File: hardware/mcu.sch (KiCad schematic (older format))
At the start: 49 parts, among them P3 CONN_01X08_DEBUG, P4 CONN_02X05_JTAG, P5 CONN_01X03_UART, P6 CONN_01X03_CAN, P7 CONN_01X05_ENCODER, SW2 SW_PUSH, U13 TM4C1294KCPDT, U14 74LVCH2T45, U15 SN65HVD231D, Y1 NX5032GA

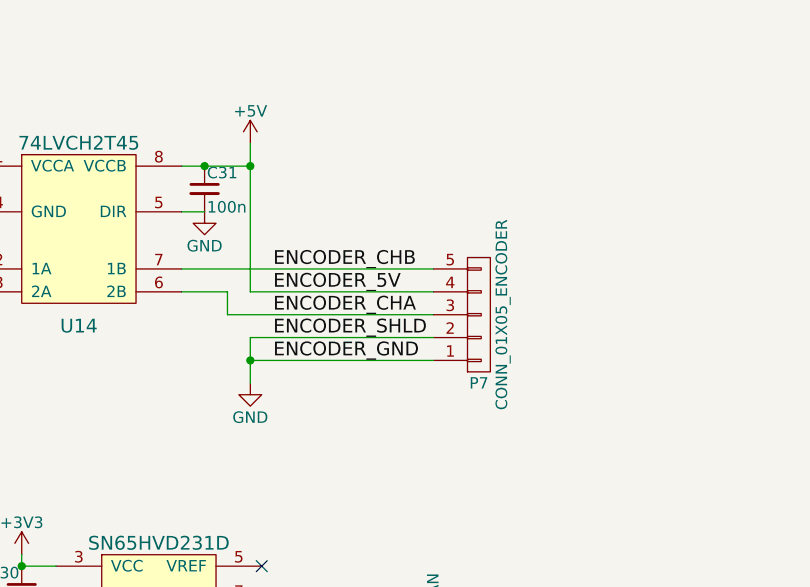
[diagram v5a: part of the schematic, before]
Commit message: Inrush circuit, mounting hole position, temp sensor
- Split inrush circuit (one for each bulk cap). Replaced NTC
  thermistor with 2W power resistor. Replaced D2Pak MOSFET with
  LFPAK MOSFETs.
- Approximate position of mechanical holes chosen.
- Added thermistor temp sensor circuits.
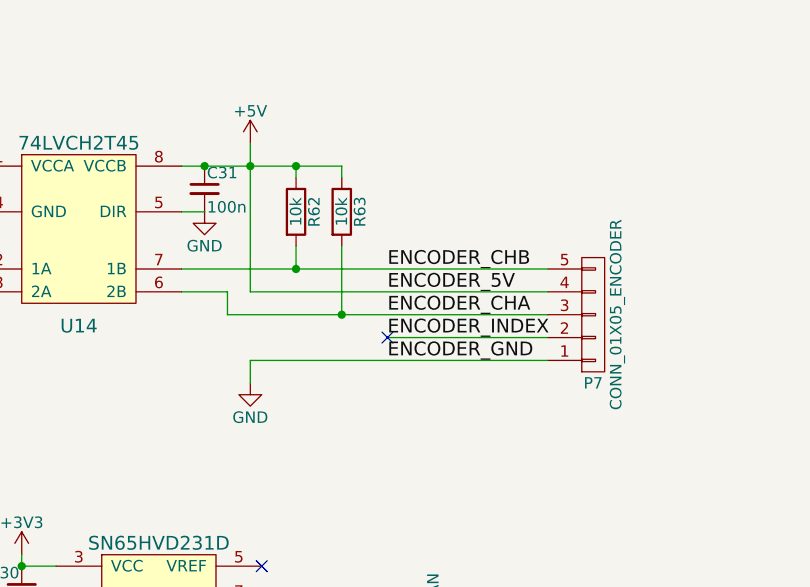
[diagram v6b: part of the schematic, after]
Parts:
- added R62, R63: 10k, Resistors_SMD:R_0603, symbol R
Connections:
- net +5V: now also R62.1, R63.1
- net ENCODER_CHA: now also R63.2
- net ENCODER_CHB: now also R62.2
- net GND: no longer P7.2 (P2)
- new net ENCODER_INDEX: P7.2 (P2)
- no-connect marks 9 -> 10
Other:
- moved on the sheet: P7
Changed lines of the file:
@@
 $EndDescr
 $Comp
-L GND #PWR77
+L GND #PWR062
 U 1 1 5983EA5A
 P 10600 1600
-F 0 "#PWR77" H 10600 1350 50  0001 C CNN
+F 0 "#PWR062" H 10600 1350 50  0001 C CNN
 F 1 "GND" H 10600 1450 50  0000 C CNN
 F 2 "" H 10600 1600 50  0000 C CNN
@@
 $EndComp
 $Comp
-L GNDA #PWR79
+L GNDA #PWR063
 U 1 1 5983EB4E
 P 10600 2700
-F 0 "#PWR79" H 10600 2450 50  0001 C CNN
+F 0 "#PWR063" H 10600 2450 50  0001 C CNN
 F 1 "GNDA" H 10600 2550 50  0000 C CNN
 F 2 "" H 10600 2700 50  0000 C CNN
@@
 $EndComp
 $Comp
-L +3.3V #PWR73
+L +3.3V #PWR064
 U 1 1 5983EC7E
 P 9200 1000
-F 0 "#PWR73" H 9200 850 50  0001 C CNN
+F 0 "#PWR064" H 9200 850 50  0001 C CNN
 F 1 "+3.3V" H 9200 1140 50  0000 C CNN
 F 2 "" H 9200 1000 50  0000 C CNN
@@
 $EndComp
 $Comp
-L GND #PWR69
+L GND #PWR065
 U 1 1 59A52C89
 P 8100 3100
-F 0 "#PWR69" H 8100 2850 50  0001 C CNN
+F 0 "#PWR065" H 8100 2850 50  0001 C CNN
 F 1 "GND" H 8100 2950 50  0000 C CNN
 F 2 "" H 8100 3100 50  0000 C CNN
@@
 $EndComp
 $Comp
-L GND #PWR70
+L GND #PWR066
 U 1 1 59A54DA4
 P 8200 1500
-F 0 "#PWR70" H 8200 1250 50  0001 C CNN
+F 0 "#PWR066" H 8200 1250 50  0001 C CNN
 F 1 "GND" H 8200 1350 50  0000 C CNN
 F 2 "" H 8200 1500 50  0000 C CNN
@@
 $EndComp
 $Comp
-L GND #PWR71
+L GND #PWR067
 U 1 1 59A55140
 P 8200 2200
-F 0 "#PWR71" H 8200 1950 50  0001 C CNN
+F 0 "#PWR067" H 8200 1950 50  0001 C CNN
 F 1 "GND" H 8200 2050 50  0000 C CNN
 F 2 "" H 8200 2200 50  0000 C CNN
@@
 $EndComp
 $Comp
-L +3.3V #PWR68
+L +3.3V #PWR068
 U 1 1 59A5A7F1
 P 8050 4550
-F 0 "#PWR68" H 8050 4400 50  0001 C CNN
+F 0 "#PWR068" H 8050 4400 50  0001 C CNN
 F 1 "+3.3V" H 8050 4690 50  0000 C CNN
 F 2 "" H 8050 4550 50  0000 C CNN
@@
 $EndComp
 $Comp
-L GND #PWR67
+L GND #PWR069
 U 1 1 59A5D67D
 P 7300 5450
-F 0 "#PWR67" H 7300 5200 50  0001 C CNN
+F 0 "#PWR069" H 7300 5200 50  0001 C CNN
 F 1 "GND" H 7300 5300 50  0000 C CNN
 F 2 "" H 7300 5450 50  0000 C CNN
@@
 $EndComp
 $Comp
-L GND #PWR75
+L GND #PWR070
 U 1 1 59A610DA
 P 10150 6200
-F 0 "#PWR75" H 10150 5950 50  0001 C CNN
+F 0 "#PWR070" H 10150 5950 50  0001 C CNN
 F 1 "GND" H 10150 6050 50  0000 C CNN
 F 2 "" H 10150 6200 50  0000 C CNN
@@
 JTAG_TDO
 $Comp
-L GND #PWR72
+L GND #PWR071
 U 1 1 59A66E5A
 P 8400 4900
-F 0 "#PWR72" H 8400 4650 50  0001 C CNN
+F 0 "#PWR071" H 8400 4650 50  0001 C CNN
 F 1 "GND" H 8400 4750 50  0000 C CNN
 F 2 "" H 8400 4900 50  0000 C CNN
@@
 $EndComp
 $Comp
-L GND #PWR74
+L GND #PWR072
 U 1 1 59A6A0A9
 P 9950 5150
-F 0 "#PWR74" H 9950 4900 50  0001 C CNN
+F 0 "#PWR072" H 9950 4900 50  0001 C CNN
 F 1 "GND" H 9950 5000 50  0000 C CNN
 F 2 "" H 9950 5150 50  0000 C CNN
@@
 $EndComp
 $Comp
-L +3V3 #PWR52
+L +3V3 #PWR073
 U 1 1 59A6BEC7
 P 800 6450
-F 0 "#PWR52" H 800 6300 50  0001 C CNN
+F 0 "#PWR073" H 800 6300 50  0001 C CNN
 F 1 "+3V3" H 800 6590 50  0000 C CNN
 F 2 "" H 800 6450 50  0000 C CNN
@@
 $EndComp
 $Comp
-L GND #PWR53
+L GND #PWR074
 U 1 1 59A6C6A6
 P 800 7350
-F 0 "#PWR53" H 800 7100 50  0001 C CNN
+F 0 "#PWR074" H 800 7100 50  0001 C CNN
 F 1 "GND" H 800 7200 50  0000 C CNN
 F 2 "" H 800 7350 50  0000 C CNN
@@
 $EndComp
 $Comp
-L GND #PWR76
+L GND #PWR075
 U 1 1 59AC0041
 P 10300 5150
-F 0 "#PWR76" H 10300 4900 50  0001 C CNN
+F 0 "#PWR075" H 10300 4900 50  0001 C CNN
 F 1 "GND" H 10300 5000 50  0000 C CNN
 F 2 "" H 10300 5150 50  0000 C CNN
@@
 $EndComp
 $Comp
-L +3VA #PWR78
+L +3VA #PWR076
 U 1 1 59B1C04F
 P 10600 2100
-F 0 "#PWR78" H 10600 1950 50  0001 C CNN
+F 0 "#PWR076" H 10600 1950 50  0001 C CNN
 F 1 "+3VA" H 10600 2240 50  0000 C CNN
 F 2 "" H 10600 2100 50  0000 C CNN
@@
 $EndComp
 $Comp
-L +3V3A #PWR80
+L +3V3A #PWR077
 U 1 1 59B1C11F
 P 10850 2250
-F 0 "#PWR80" H 10850 2100 50  0001 C CNN
+F 0 "#PWR077" H 10850 2100 50  0001 C CNN
 F 1 "+3V3A" H 10850 2390 50  0000 C CNN
 F 2 "" H 10850 2250 50  0000 C CNN
@@
 $EndComp
 $Comp
-L GND #PWR58
+L GND #PWR078
 U 1 1 59BBDFC5
 P 3350 6750
-F 0 "#PWR58" H 3350 6500 50  0001 C CNN
+F 0 "#PWR078" H 3350 6500 50  0001 C CNN
 F 1 "GND" H 3350 6600 50  0000 C CNN
 F 2 "" H 3350 6750 50  0000 C CNN
@@
 $EndComp
 $Comp
-L +3V3 #PWR57
+L +3V3 #PWR079
 U 1 1 59BBFAFC
 P 3350 6500
-F 0 "#PWR57" H 3350 6350 50  0001 C CNN
+F 0 "#PWR079" H 3350 6350 50  0001 C CNN
 F 1 "+3V3" H 3350 6640 50  0000 C CNN
 F 2 "" H 3350 6500 50  0000 C CNN
@@
 $EndComp
 $Comp
-L GND #PWR63
+L GND #PWR080
 U 1 1 59BC34FC
 P 4450 7550
-F 0 "#PWR63" H 4450 7300 50  0001 C CNN
+F 0 "#PWR080" H 4450 7300 50  0001 C CNN
 F 1 "GND" H 4450 7400 50  0000 C CNN
 F 2 "" H 4450 7550 50  0000 C CNN
@@
 L CONN_01X05 P7
 U 1 1 59C3A0F4
-P 5350 5450
-F 0 "P7" H 5350 5750 50  0000 C CNN
-F 1 "CONN_01X05_ENCODER" V 5450 5450 50  0000 C CNN
-F 2 "2kwMotorController:TERM_5P_2-5_1990038" H 5350 5450 50  0001 C CNN
-F 3 "" H 5350 5450 50  0000 C CNN
-	1    5350 5450
+P 5850 5450
+F 0 "P7" H 5850 5750 50  0000 C CNN
+F 1 "CONN_01X05_ENCODER" V 5950 5450 50  0000 C CNN
+F 2 "2kwMotorController:TERM_5P_2-5_1990038" H 5850 5450 50  0001 C CNN
+F 3 "" H 5850 5450 50  0000 C CNN
+	1    5850 5450
 	1    0    0    1
 $EndComp
-Text Label 4450 5450 0    60   ~ 0
+Text Label 4950 5450 0    60   ~ 0
 ENCODER_CHA
-Text Label 4450 5250 0    60   ~ 0
+Text Label 4950 5250 0    60   ~ 0
 ENCODER_CHB
 $Comp
-L +5V #PWR61
+L +5V #PWR081
 U 1 1 59C3A102
 P 4350 4700
-F 0 "#PWR61" H 4350 4550 50  0001 C CNN
+F 0 "#PWR081" H 4350 4550 50  0001 C CNN
 F 1 "+5V" H 4350 4840 50  0000 C CNN
 F 2 "" H 4350 4700 50  0000 C CNN
@@
 $EndComp
 $Comp
-L GND #PWR62
+L GND #PWR082
 U 1 1 59C3A10A
 P 4350 5750
-F 0 "#PWR62" H 4350 5500 50  0001 C CNN
+F 0 "#PWR082" H 4350 5500 50  0001 C CNN
 F 1 "GND" H 4350 5600 50  0000 C CNN
 F 2 "" H 4350 5750 50  0000 C CNN
@@
 	-1   0    0    -1
 $EndComp
-Text Label 4450 5350 0    60   ~ 0
+Text Label 4950 5350 0    60   ~ 0
 ENCODER_5V
-Text Label 4450 5650 0    60   ~ 0
+Text Label 4950 5650 0    60   ~ 0
 ENCODER_GND
-Text Label 4450 5550 0    60   ~ 0
-ENCODER_SHLD
+Text Label 4950 5550 0    60   ~ 0
+ENCODER_INDEX
 Wire Wire Line
 	10500 1050 10600 1050
@@
 	1300 3850 1850 3850
 Wire Wire Line
-	4350 5350 5150 5350
-Wire Wire Line
-	4050 5250 5150 5250
+	4350 5350 5650 5350
+Wire Wire Line
+	4050 5250 5650 5250
 Text Label 2900 7150 0    60   ~ 0
 CAN_RX
@@
 	1800 4850 1800 5800
 $Comp
-L GND #PWR54
+L GND #PWR083
 U 1 1 59C4EEA9
 P 1800 5800
-F 0 "#PWR54" H 1800 5550 50  0001 C CNN
+F 0 "#PWR083" H 1800 5550 50  0001 C CNN
 F 1 "GND" H 1800 5650 50  0000 C CNN
 F 2 "" H 1800 5800 50  0000 C CNN
@@
 $EndComp
 $Comp
-L GND #PWR59
+L GND #PWR084
 U 1 1 59C713F3
 P 3950 600
-F 0 "#PWR59" H 3950 350 50  0001 C CNN
+F 0 "#PWR084" H 3950 350 50  0001 C CNN
 F 1 "GND" H 3950 450 50  0000 C CNN
 F 2 "" H 3950 600 50  0000 C CNN
@@
 	4800 7000 4800 7050
 $Comp
-L GND #PWR65
+L GND #PWR085
 U 1 1 59C7E547
 P 4800 7050
-F 0 "#PWR65" H 4800 6800 50  0001 C CNN
+F 0 "#PWR085" H 4800 6800 50  0001 C CNN
 F 1 "GND" H 4800 6900 50  0000 C CNN
 F 2 "" H 4800 7050 50  0000 C CNN
@@
 Connection ~ 4800 2000
 $Comp
-L GND #PWR64
+L GND #PWR086
 U 1 1 59B94400
 P 4800 2050
-F 0 "#PWR64" H 4800 1800 50  0001 C CNN
+F 0 "#PWR086" H 4800 1800 50  0001 C CNN
 F 1 "GND" H 4800 1900 50  0000 C CNN
 F 2 "" H 4800 2050 50  0000 C CNN
@@
 $EndComp
 Wire Wire Line
-	4350 5650 5150 5650
-Wire Wire Line
-	4350 5550 4350 5750
+	4350 5650 5650 5650
 Wire Wire Line
 	4350 4700 4350 5350
-Connection ~ 4350 5650
-Wire Wire Line
-	4350 5550 5150 5550
-Wire Wire Line
-	4250 5450 5150 5450
+Wire Wire Line
+	4250 5450 5650 5450
 Wire Wire Line
 	4050 5350 4250 5350
@@
 $EndComp
 $Comp
-L GND #PWR60
+L GND #PWR087
 U 1 1 59BE4ED0
 P 4150 5000
-F 0 "#PWR60" H 4150 4750 50  0001 C CNN
+F 0 "#PWR087" H 4150 4750 50  0001 C CNN
 F 1 "GND" H 4150 4850 50  0000 C CNN
 F 2 "" H 4150 5000 50  0000 C CNN
@@
 	4050 5000 4150 5000
 Wire Wire Line
-	4050 4800 4350 4800
+	4050 4800 4750 4800
 Connection ~ 4350 4800
 Connection ~ 4150 4800
@@
 	3150 4800 3050 4800
 $Comp
-L GND #PWR56
+L GND #PWR088
 U 1 1 59BEB29C
 P 3050 5000
-F 0 "#PWR56" H 3050 4750 50  0001 C CNN
+F 0 "#PWR088" H 3050 4750 50  0001 C CNN
 F 1 "GND" H 3050 4850 50  0000 C CNN
 F 2 "" H 3050 5000 50  0000 C CNN
@@
 QEI_PHB
 $Comp
-L +3V3 #PWR55
+L +3V3 #PWR089
 U 1 1 59BF12ED
 P 3050 4700
-F 0 "#PWR55" H 3050 4550 50  0001 C CNN
+F 0 "#PWR089" H 3050 4550 50  0001 C CNN
 F 1 "+3V3" H 3050 4840 50  0000 C CNN
 F 2 "" H 3050 4700 50  0000 C CNN
@@
 	6950 1050 7050 1050
 $Comp
-L GND #PWR66
+L GND #PWR090
 U 1 1 59C1E162
 P 7300 1100
-F 0 "#PWR66" H 7300 850 50  0001 C CNN
+F 0 "#PWR090" H 7300 850 50  0001 C CNN
 F 1 "GND" H 7300 950 50  0000 C CNN
 F 2 "" H 7300 1100 50  0000 C CNN
@@
 Text Notes 6950 900  0    60   ~ 0
 CONNECT TO ENABLE\nFACTORY RESET ON\nNEXT SYSTEM RESET
+$Comp
+L R R62
+U 1 1 59C1BB00
+P 4550 5000
+F 0 "R62" V 4630 5000 50  0000 C CNN
+F 1 "10k" V 4550 5000 50  0000 C CNN
+F 2 "Resistors_SMD:R_0603" V 4480 5000 50  0001 C CNN
+F 3 "" H 4550 5000 50  0000 C CNN
+	1    4550 5000
+	1    0    0    -1
+$EndComp
+$Comp
+L R R63
+U 1 1 59C1BD50
+P 4750 5000
+F 0 "R63" V 4830 5000 50  0000 C CNN
+F 1 "10k" V 4750 5000 50  0000 C CNN
+F 2 "Resistors_SMD:R_0603" V 4680 5000 50  0001 C CNN
+F 3 "" H 4750 5000 50  0000 C CNN
+	1    4750 5000
+	1    0    0    -1
+$EndComp
+Wire Wire Line
+	4550 5150 4550 5250
+Connection ~ 4550 5250
+Wire Wire Line
+	4750 5150 4750 5450
+Connection ~ 4750 5450
+Wire Wire Line
+	4750 4800 4750 4850
+Wire Wire Line
+	4550 4850 4550 4800
+Connection ~ 4550 4800
+Wire Wire Line
+	4350 5750 4350 5650
+Wire Wire Line
+	4950 5550 5650 5550
+NoConn ~ 4950 5550
 $EndSCHEMATC

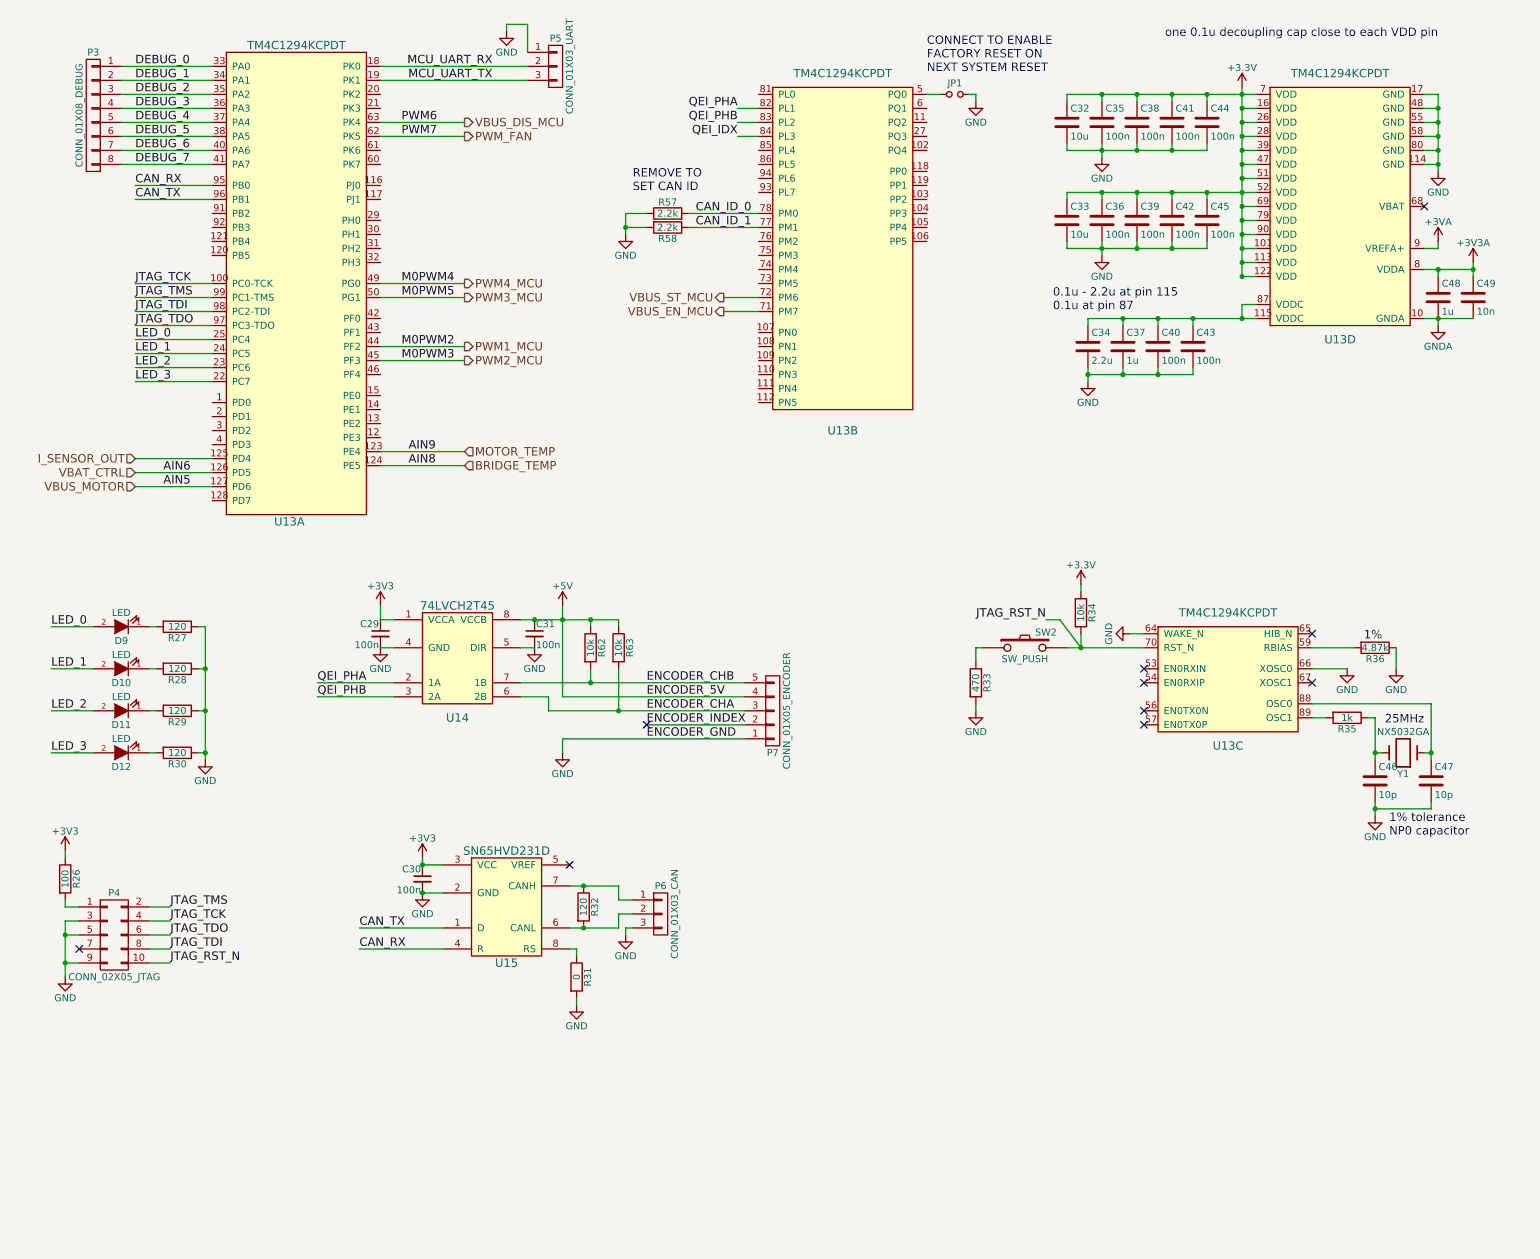
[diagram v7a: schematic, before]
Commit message: Draft layout of controller section
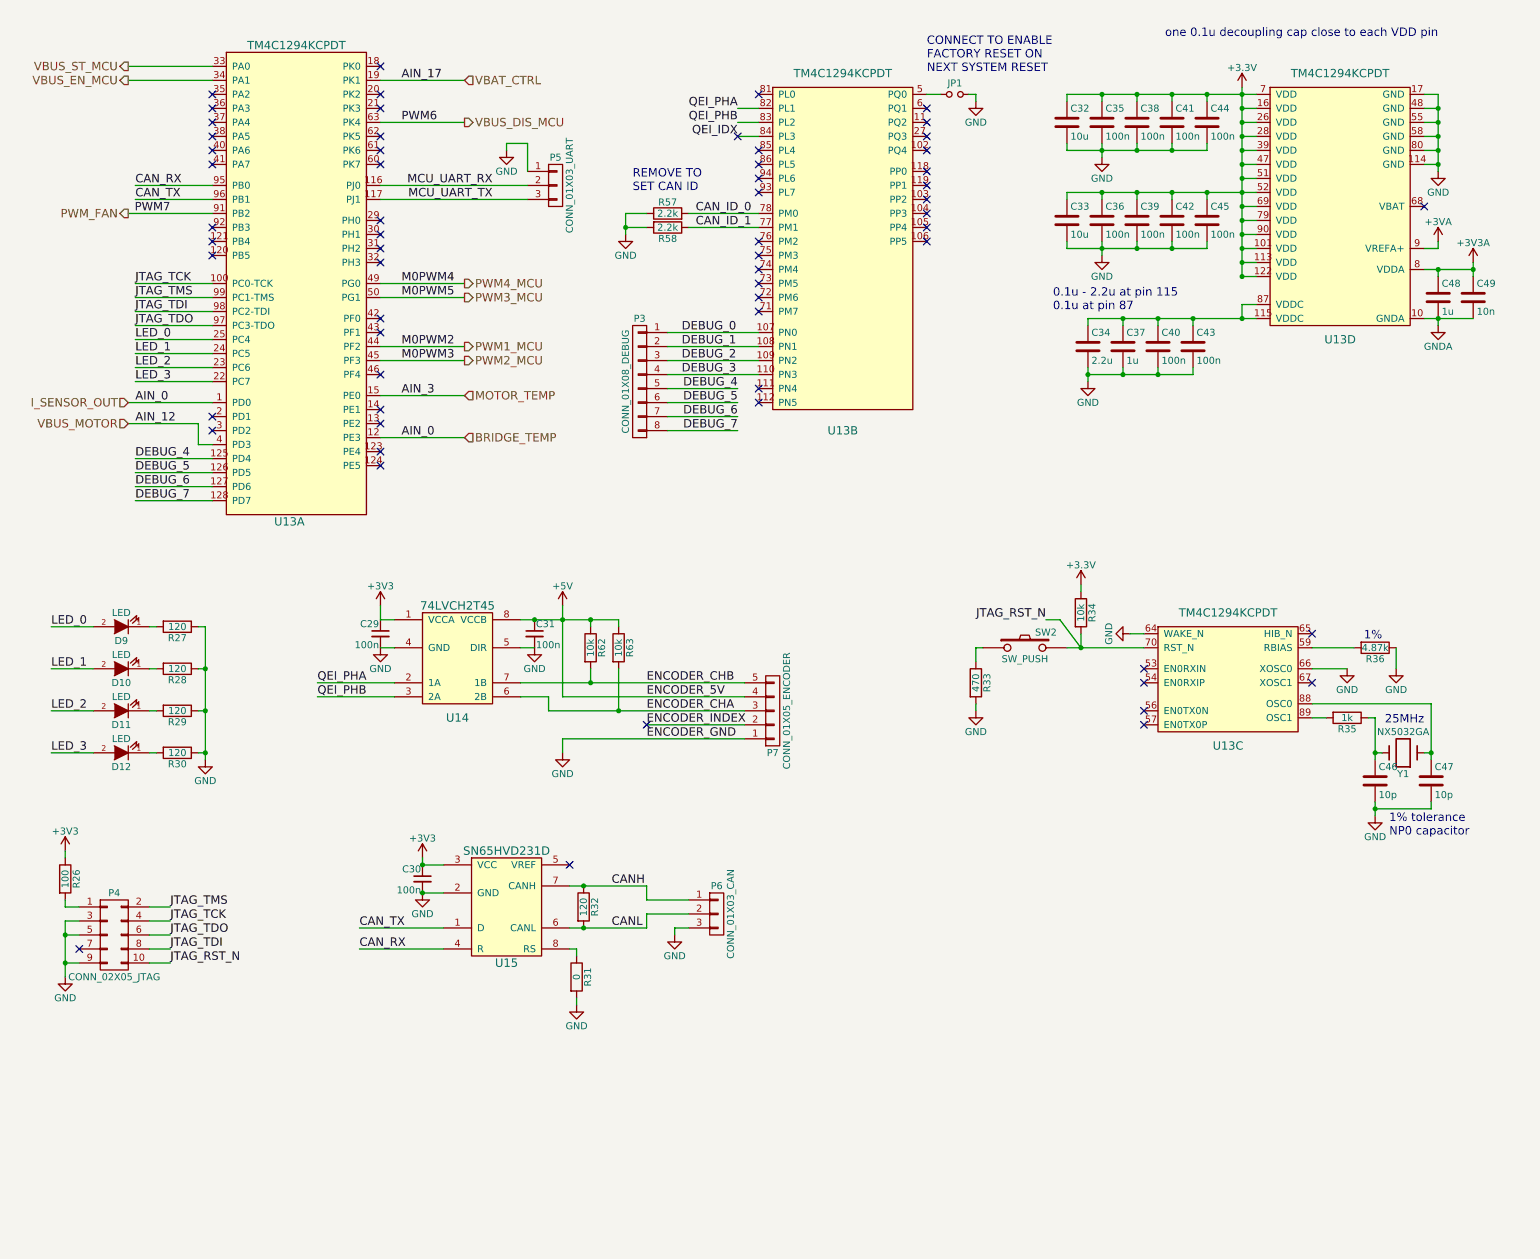
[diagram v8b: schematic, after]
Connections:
- net I_SENSOR_OUT is gone; now on net DEBUG_4: U13.125 (PD4)
- net BRIDGE_TEMP: now also U13.1 (PD0), U13.12 (PE3); no longer U13.124 (PE5)
- net DEBUG_0: now also U13.107 (PN0); no longer U13.33 (PA0)
- net DEBUG_1: now also U13.108 (PN1); no longer U13.34 (PA1)
- net DEBUG_2: now also U13.109 (PN2); no longer U13.35 (PA2)
- net DEBUG_3: now also U13.110 (PN3); no longer U13.36 (PA3)
- net DEBUG_4: no longer U13.37 (PA4)
- net DEBUG_5: now also U13.126 (PD5); no longer U13.38 (PA5)
- net DEBUG_6: now also U13.127 (PD6); no longer U13.40 (PA6)
- net DEBUG_7: now also U13.128 (PD7); no longer U13.41 (PA7)
- net MCU_UART_RX: now also U13.116 (PJ0); no longer U13.18 (PK0)
- net MCU_UART_TX: now also U13.117 (PJ1); no longer U13.19 (PK1)
- net MOTOR_TEMP: now also U13.15 (PE0); no longer U13.123 (PE4)
- net PWM_FAN: now also U13.91 (PB2); no longer U13.62 (PK5)
- net VBAT_CTRL: now also U13.19 (PK1); no longer U13.126 (PD5)
- net VBUS_EN_MCU: now also U13.34 (PA1); no longer U13.71 (PM7)
- net VBUS_MOTOR: now also U13.4 (PD3); no longer U13.127 (PD6)
- net VBUS_ST_MCU: now also U13.33 (PA0); no longer U13.72 (PM6)
- net CANL: now reaches P6.2 (P2), R32.2, U15.6 (CANL)
- net CANH: now reaches P6.1 (P1), R32.1, U15.7 (CANH)
- no-connect marks 10 -> 62
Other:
- moved on the sheet: P3, P5, P6
